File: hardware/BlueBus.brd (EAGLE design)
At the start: 90 x 60 mm, 135 parts, among them Q1 NMOSFET-BSS138K, Q2 PMOSFET-DMP1045UQ, Q3 NMOSFET-BSS138K, X1 CRYSTAL-12MHZ

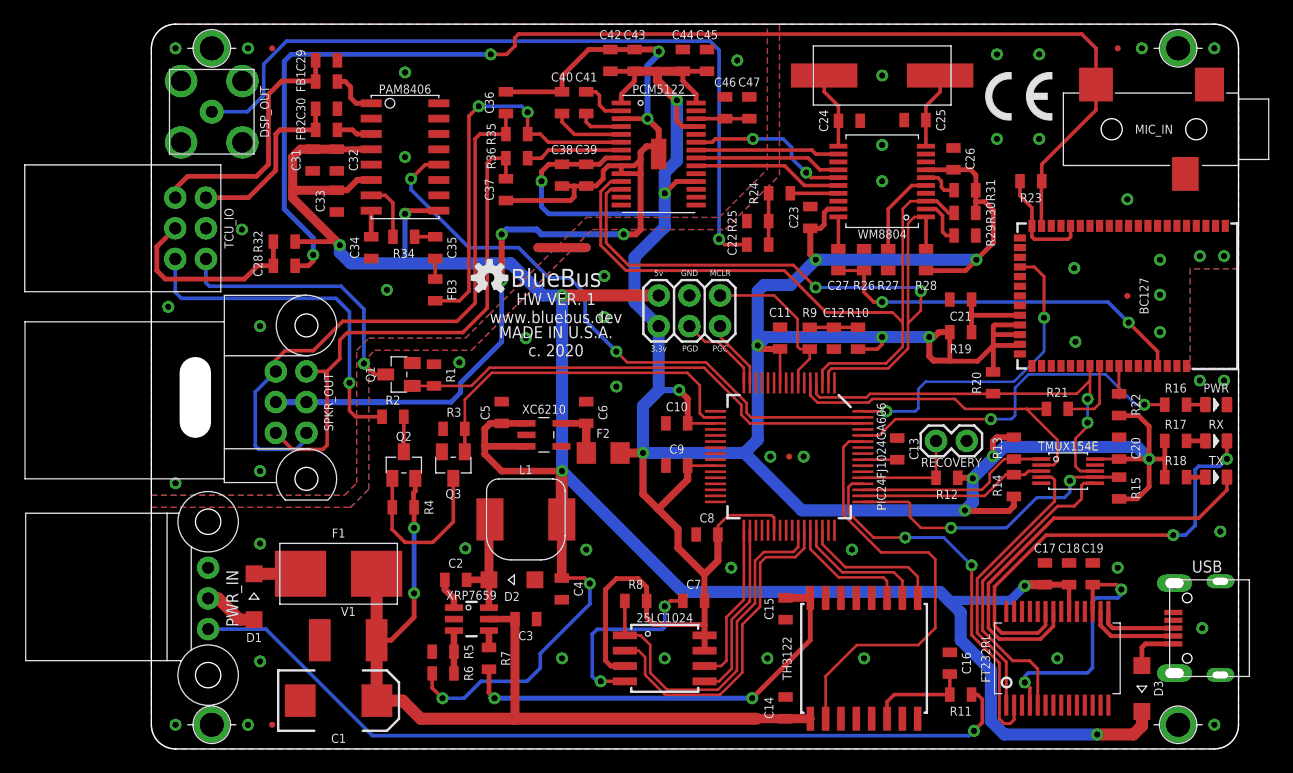
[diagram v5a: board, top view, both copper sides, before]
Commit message: [IMP] hardware: V 1.1 * Reroute 3.3v rail under the PIC24 to prevent ground returns on the second layer from having to take a longer route * Bring 5v rail to top layer for a short run in order to open the ground return path (to the left of the PIC24) * Leave pin 3 of the SPKR_OUT connector floating to prevent audio channel grounding on certain models * Add space between the edge of the analog audio ground plane end and the R/L channel traces * VIA stitch layers around the ground "bridge" (right above the BlueBus name on the Silkscreen) * Increase GND bridge to 1mm from 0.75mm * Increase BC127 pad size to allow more paste to fill the castellations * Bring RC filter for BC127 closer to power pin
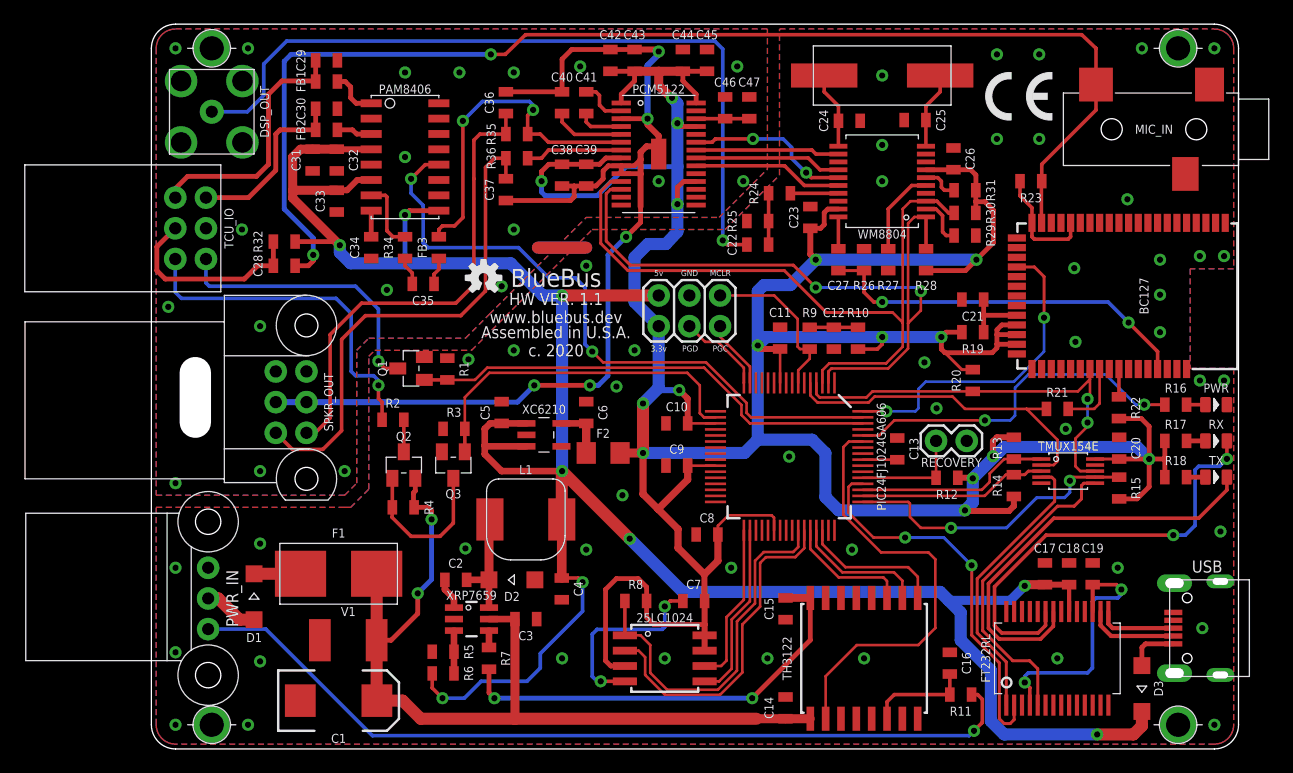
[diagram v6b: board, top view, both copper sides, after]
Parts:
- removed FID1, FID2, FID3, FID4, FID5: FIDUCIAL_0.5MM, MF_Aesthetics:FIDUCIAL_0.5MM
- moved FB3 3.51 mm to (23.8, 41.5), turned to 270 degrees
- moved C35 3.16 mm to (22.5, 38.5), turned to 180 degrees
- moved R20 1.69 mm to (68.0, 30.5)
- moved R1 1.21 mm to (24.5, 31.4)
- moved Q1 1.12 mm to (21.5, 31.5)
- moved C21 1.00 mm to (68.0, 37.2)
- moved R19 1.00 mm to (68.0, 34.5)
- moved R34 0.91 mm to (21.0, 41.5), turned to 90 degrees
- moved OSHW 0.50 mm to (27.5, 39.0)
- moved R22 0.25 mm to (80.1, 28.2)
- moved R2 0.25 mm to (20.0, 27.2)
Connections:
- net SPKR_OUT_L: no longer SPKR_OUT.6
- net SPKR_OUT_R: no longer SPKR_OUT.3
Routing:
- net SPKR_OUT_L: track 49.5 -> 39.5 mm
- net DAC_OUT_L: track 32.9 -> 28.2 mm
- net TEL_AMP_SHDN: track 50.7 -> 54.1 mm
- net SPKR_OUT_R: track 44.5 -> 41.7 mm
- net 3.3V: track 319.4 -> 316.7 mm, vias 14 -> 16
- net VIN: track 72.9 -> 74.8 mm
- net BT_3V3_FILTER: track 6.70 -> 5.45 mm
- net MCU_TEL_MUTE: track 40.3 -> 39.1 mm
- net TEL_AMP_INL: track 4.86 -> 5.86 mm
- net TEL_ON_EN: track 14.1 -> 13.1 mm
- net 5V: track 199.2 -> 198.4 mm, vias 8 -> 9
- net TEL_MUTE_IO: track 22.6 -> 23.3 mm
- net TEL_AMP_INL_CAP_RES: track 1.70 -> 2.35 mm
- net BT_RST: track 2.94 -> 2.30 mm
- net TEL_AMP_IN: track 1.70 -> 2.27 mm
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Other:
- board text added: "Assembled in U.S.A."
- board text added: "HW VER. 1.1"
- board text added: "NC"
- board text removed: "HW VER. 1"
- board text removed: "MADE IN U.S.A."

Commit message: [IMP] hardware: V 1.2 * Power PAM8406 PVDDR and add bypass caps * Rework layout for PAM8406 and its passives * Connect floating VIAs to ground
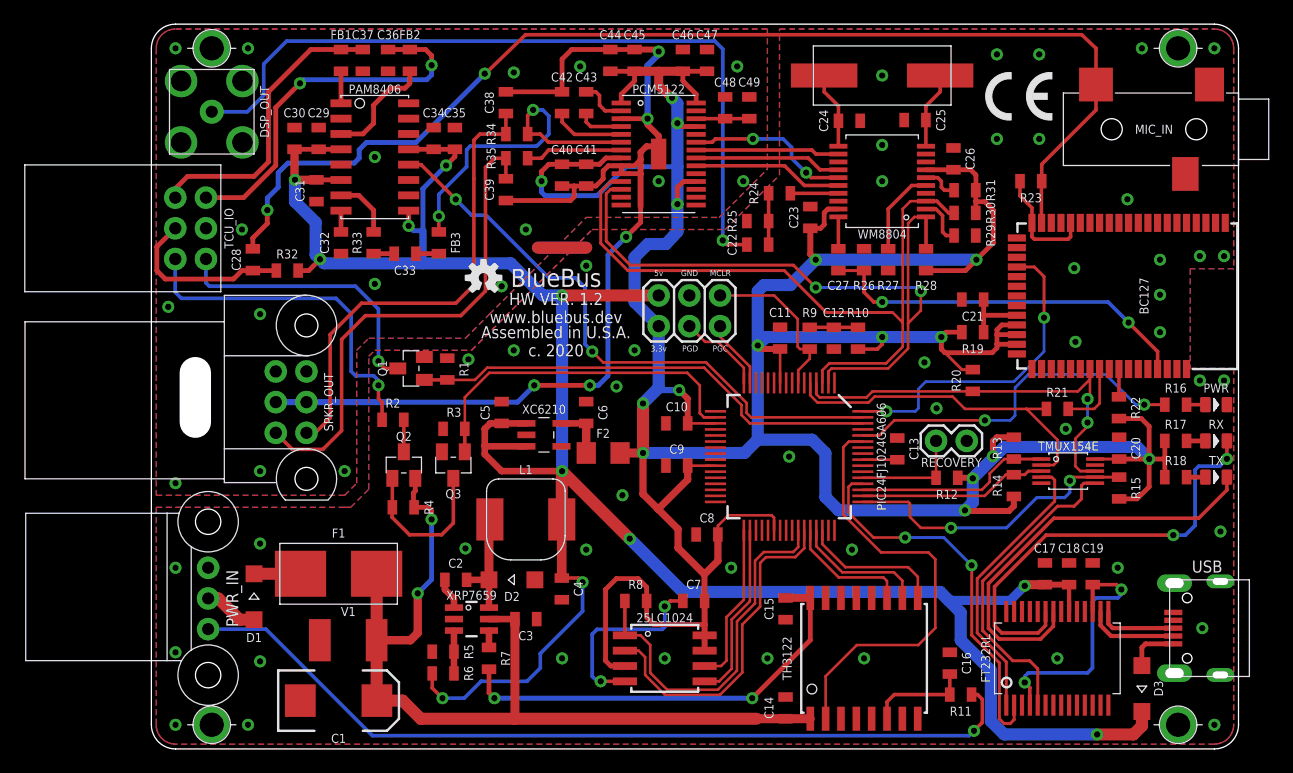
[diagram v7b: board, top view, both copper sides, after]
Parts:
- removed R36: 110, Passives:0805
- added C48: 0.1uF, Passives:0805
- added C49: 10uF, Passives:0805
- added R33: 18k, Passives:0805
- C29: value 220pF -> 10uF
- C30: value 220pF -> 1uF
- C31: value 10uF -> 1uF
- C35: value 1uF -> 10uF
- C36, C37: value 9nF -> 220pF
- C38: value 10uF -> 9nF
- C39: value 0.1uF -> 9nF
- C40: value 2.2uF -> 10uF
- C41: value 2.2uF -> 0.1uF
- C42: value 10uF -> 2.2uF
- C43: value 0.1uF -> 2.2uF
- C44: value 0.1uF -> 10uF
- C45: value 10uF -> 0.1uF
- Q2: value PMOSFET-DMP1045UQ -> PMOSFET-DMP32D4S
- R32: value 2k -> 4.7k
- R34: value 18k -> 110
- moved C37 16.0 mm to (17.5, 57.0)
- moved R34 13.2 mm to (30.2, 50.9), turned to 180 degrees
- moved C35 12.3 mm to (25.1, 50.5), turned to 90 degrees
- moved C34 10.4 mm to (23.4, 50.5), turned to 90 degrees
- moved C36 10.4 mm to (19.6, 57.0), turned to 270 degrees
- moved FB2 8.98 mm to (21.4, 57.0), turned to 90 degrees
- moved C38 7.59 mm to (29.4, 53.5), turned to 90 degrees
- moved C33 7.13 mm to (21.0, 41.0), turned to 180 degrees
- moved C29 6.98 mm to (11.8, 50.5), turned to 90 degrees
- moved C32 6.86 mm to (15.7, 41.9)
- moved C39 6.76 mm to (29.4, 46.3)
- moved C40 6.00 mm to (34.0, 47.5)
- moved C41 6.00 mm to (36.0, 47.5)
- moved C44 6.00 mm to (38.0, 57.0)
- moved C45 6.00 mm to (40.0, 57.0)
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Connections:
- net 3.3V: now also C40.1, C41.1, C46.1, C47.1; no longer C38.1, C39.1, C42.1, C43.1
- net 5V: now also C29.1, C30.1, C34.1, C35.1, PAM8406.13; no longer C32.1, C33.1
- net AGND: now also C40.2, C41.2, C42.1, C44.2, C45.2; no longer C36.2, C37.2, C40.1, C42.2, C43.2
- net DAC_CAPM: now also C43.2; no longer C41.2
- net DAC_CAPP: now also C43.1; no longer C41.1
- net DAC_LDOO: now also C48.1, C49.1; no longer C46.1, C47.1
- net DAC_OUT_L: now also R34.1; no longer R35.1
- net DAC_OUT_R: now also R35.1; no longer R36.1
- net DAC_VNEG: now also C42.2; no longer C40.2
- net GND: now also C35.2, C36.2, C37.2, C48.2, C49.2; no longer C33.2, C44.2, C45.2
- net SPKR_OUT_L: now also C38.1, R34.2; no longer C36.1, R35.2
- net SPKR_OUT_R: now also C39.1, R35.2; no longer C37.1, R36.2
- net TEL_AMP_IN: now also C33.1; no longer C35.1
- net TEL_AMP_INL: now also R33.2; no longer R34.2
- net TEL_AMP_INL_CAP_RES: now also C33.2, R33.1; no longer C35.2, R34.1
- net TEL_AMP_VREF: now also C32.1; no longer C34.1
- net TEL_OUT_L+: now also C37.1; no longer C29.1
- net TEL_OUT_L-: now also C36.1; no longer C30.1
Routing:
- net TEL_OUT_L-: track 14.9 -> 31.1 mm, vias 0 -> 2
- net BT_MIC_L: track 105.0 -> 97.7 mm
- net TEL_AMP_OUT_L-: track 3.13 -> 9.31 mm
- net TEL_AMP_SHDN: track 54.1 -> 49.5 mm
- net 5V: track 198.4 -> 202.7 mm, vias 9 -> 11
- net TEL_OUT_L+: track 21.2 -> 24.4 mm
- net TEL_MIC_L_OUT: track 16.5 -> 14.6 mm
- net TEL_AMP_OUT_L+: track 4.07 -> 2.65 mm
- net VIN: track 74.8 -> 75.7 mm
- net TEL_AMP_INL: track 5.86 -> 5.01 mm
- net TEL_AMP_INL_CAP_RES: track 2.35 -> 1.70 mm
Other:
- board text added: "HW VER. 1.2"
- board text removed: "HW VER. 1.1"
